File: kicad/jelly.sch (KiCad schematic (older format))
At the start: 30 parts, among them M1 PAGER_MOTOR, M2 PAGER_MOTOR, P1 CONN_01X01, P10 CONN_01X01, P11 CONN_01X01, P12 CONN_01X01, P13 CONN_01X01, P14 CONN_01X01, P15 CONN_01X01, P2 CONN_01X01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

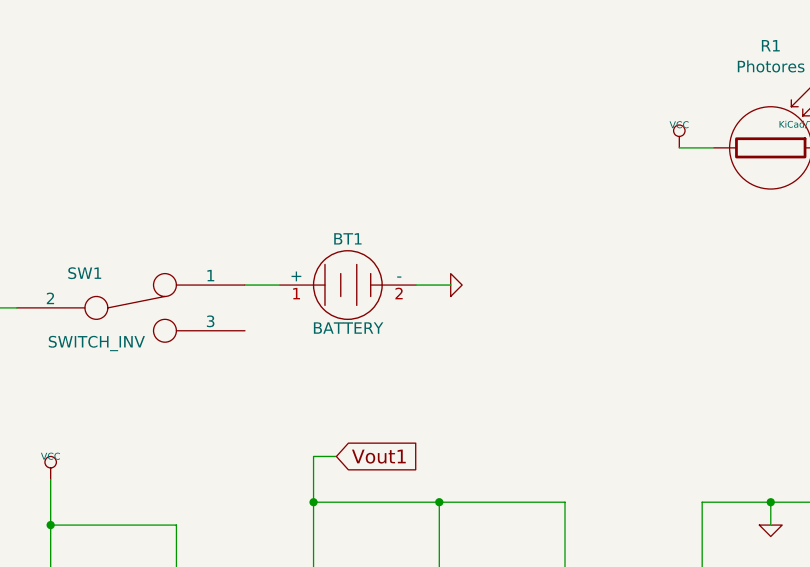
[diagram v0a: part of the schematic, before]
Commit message: Give up on CR2450
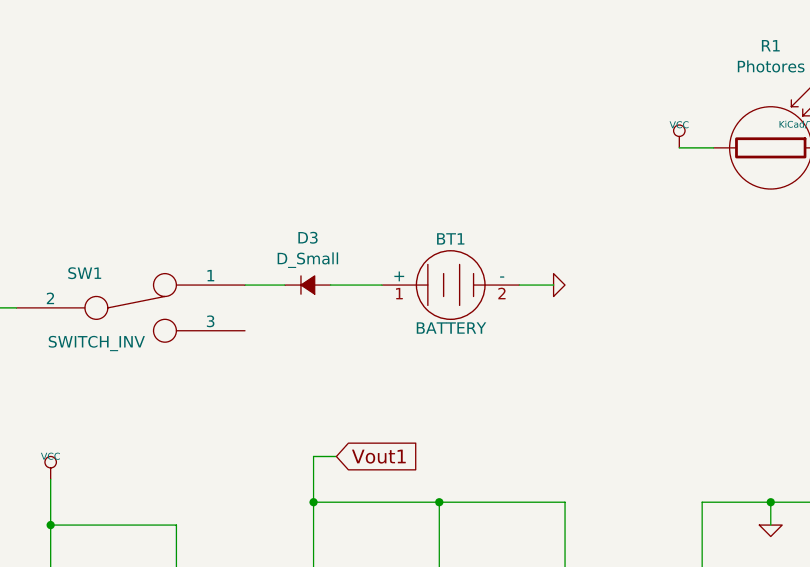
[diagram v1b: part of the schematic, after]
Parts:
- added D3: D_Small, KiCad/Diodes_ThroughHole.pretty:Diode_DO-41_SOD81_Horizontal_RM10, symbol D_Small
- BT1: footprint custom:cr2450_holder -> KiCad/Pin_Headers.pretty:Pin_Header_Straight_1x02
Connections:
- wire segments 48 -> 49
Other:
- moved on the sheet: BT1
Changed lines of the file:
@@
 L BATTERY BT1
 U 1 1 57C0D38C
-P 2750 3500
-F 0 "BT1" H 2750 3700 50  0000 C CNN
-F 1 "BATTERY" H 2750 3310 50  0000 C CNN
-F 2 "custom:cr2450_holder" H 2750 3500 60  0001 C CNN
-F 3 "~" H 2750 3500 60  0000 C CNN
-	1    2750 3500
+P 3200 3500
+F 0 "BT1" H 3200 3700 50  0000 C CNN
+F 1 "BATTERY" H 3200 3310 50  0000 C CNN
+F 2 "KiCad/Pin_Headers.pretty:Pin_Header_Straight_1x02" H 3200 3500 60  0001 C CNN
+F 3 "~" H 3200 3500 60  0000 C CNN
+	1    3200 3500
 	1    0    0    -1
 $EndComp
@@
 L GND-RESCUE-bristle_bot #PWR01
 U 1 1 57C0D38E
-P 3200 3500
-F 0 "#PWR01" H 3200 3500 30  0001 C CNN
-F 1 "GND" H 3200 3430 30  0001 C CNN
-F 2 "" H 3200 3500 60  0000 C CNN
-F 3 "" H 3200 3500 60  0000 C CNN
-	1    3200 3500
+P 3650 3500
+F 0 "#PWR01" H 3650 3500 30  0001 C CNN
+F 1 "GND" H 3650 3430 30  0001 C CNN
+F 2 "" H 3650 3500 60  0000 C CNN
+F 3 "" H 3650 3500 60  0000 C CNN
+	1    3650 3500
 	0    -1   -1   0
 $EndComp
@@
 	5050 2900 5050 3200
 Wire Wire Line
-	3050 3500 3200 3500
+	3500 3500 3650 3500
 Wire Wire Line
 	5350 2500 5350 2700
-Wire Wire Line
-	2450 3500 2300 3500
 Wire Wire Line
 	5050 2900 4850 2900
@@
 Wire Wire Line
 	8300 6350 8450 6350
+$Comp
+L D_Small D3
+U 1 1 57C374D3
+P 2575 3500
+F 0 "D3" H 2575 3705 50  0000 C CNN
+F 1 "D_Small" H 2575 3614 50  0000 C CNN
+F 2 "KiCad/Diodes_ThroughHole.pretty:Diode_DO-41_SOD81_Horizontal_RM10" V 2575 3500 50  0001 C CNN
+F 3 "" V 2575 3500 50  0000 C CNN
+	1    2575 3500
+	1    0    0    -1
+$EndComp
+Wire Wire Line
+	2300 3500 2475 3500
+Wire Wire Line
+	2675 3500 2900 3500
 $EndSCHEMATC

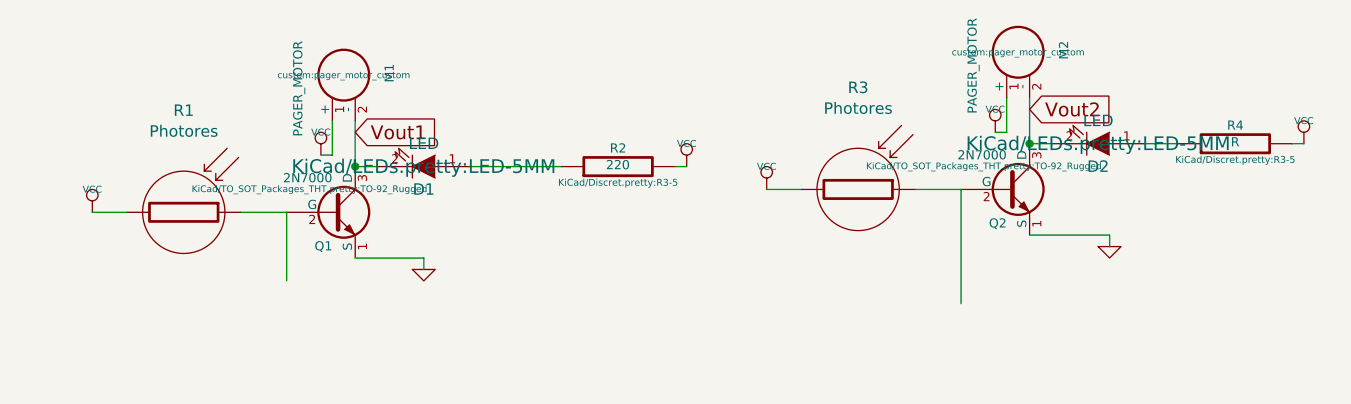
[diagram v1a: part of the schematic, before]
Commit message: Turn of visibility of footprint fields in schematic
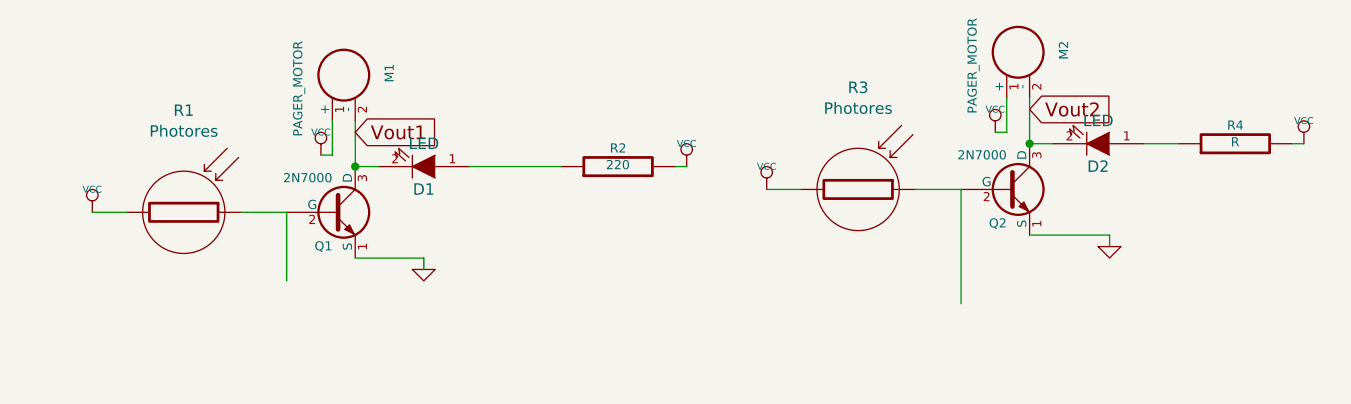
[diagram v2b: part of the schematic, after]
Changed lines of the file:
@@
 F 0 "BT1" H 3200 3700 50  0000 C CNN
 F 1 "BATTERY" H 3200 3310 50  0000 C CNN
-F 2 "KiCad/Pin_Headers.pretty:Pin_Header_Straight_1x02" H 3200 3500 60  0001 C CNN
+F 2 "KiCad/Pin_Headers.pretty:Pin_Header_Straight_1x02" H 3200 3500 29  0001 C CNN
 F 3 "~" H 3200 3500 60  0000 C CNN
 	1    3200 3500
@@
 F 0 "M1" V 5500 2350 40  0000 R CNN
 F 1 "PAGER_MOTOR" V 5100 2450 40  0000 R CNN
-F 2 "custom:pager_motor_custom" H 5300 2300 29  0000 C CNN
+F 2 "custom:pager_motor_custom" H 5300 2300 29  0001 C CNN
 F 3 "" H 5300 2300 60  0000 C CNN
 	1    5300 2300
@@
 F 0 "Q1" H 5250 2752 40  0000 R CNN
 F 1 "2N7000" H 5250 3050 40  0000 R CNN
-F 2 "KiCad/TO_SOT_Packages_THT.pretty:TO-92_Rugged" H 5150 3002 29  0000 C CNN
+F 2 "KiCad/TO_SOT_Packages_THT.pretty:TO-92_Rugged" H 5150 3002 29  0001 C CNN
 F 3 "" H 5250 2900 60  0000 C CNN
 	1    5250 2900
@@
 F 0 "#PWR02" H 1100 3700 30  0001 C CNN
 F 1 "VCC" H 1100 3700 30  0000 C CNN
-F 2 "" H 1100 3600 60  0000 C CNN
+F 2 "" H 1100 3600 60  0001 C CNN
 F 3 "" H 1100 3600 60  0000 C CNN
 	1    1100 3600
@@
 F 0 "#PWR03" H 4200 3000 30  0001 C CNN
 F 1 "VCC" H 4200 3000 30  0000 C CNN
-F 2 "" H 4200 2900 60  0000 C CNN
+F 2 "" H 4200 2900 60  0001 C CNN
 F 3 "" H 4200 2900 60  0000 C CNN
 	1    4200 2900
@@
 F 0 "#PWR04" H 5200 2750 30  0001 C CNN
 F 1 "VCC" H 5200 2750 30  0000 C CNN
-F 2 "" H 5200 2650 60  0000 C CNN
+F 2 "" H 5200 2650 60  0001 C CNN
 F 3 "" H 5200 2650 60  0000 C CNN
 	1    5200 2650
@@
 F 0 "#PWR05" H 5650 3150 30  0001 C CNN
 F 1 "GND" H 5650 3080 30  0001 C CNN
-F 2 "" H 5650 3150 60  0000 C CNN
+F 2 "" H 5650 3150 60  0001 C CNN
 F 3 "" H 5650 3150 60  0000 C CNN
 	1    5650 3150
@@
 F 0 "M2" V 8450 2250 40  0000 R CNN
 F 1 "PAGER_MOTOR" V 8050 2350 40  0000 R CNN
-F 2 "custom:pager_motor_custom" H 8250 2200 29  0000 C CNN
+F 2 "custom:pager_motor_custom" H 8250 2200 29  0001 C CNN
 F 3 "" H 8250 2200 60  0000 C CNN
 	1    8250 2200
@@
 F 0 "#PWR06" H 8150 2650 30  0001 C CNN
 F 1 "VCC" H 8150 2650 30  0000 C CNN
-F 2 "" H 8150 2550 60  0000 C CNN
+F 2 "" H 8150 2550 60  0001 C CNN
 F 3 "" H 8150 2550 60  0000 C CNN
 	1    8150 2550
@@
 F 0 "Q2" H 8200 2652 40  0000 R CNN
 F 1 "2N7000" H 8200 2950 40  0000 R CNN
-F 2 "KiCad/TO_SOT_Packages_THT.pretty:TO-92_Rugged" H 8100 2902 29  0000 C CNN
+F 2 "KiCad/TO_SOT_Packages_THT.pretty:TO-92_Rugged" H 8100 2902 29  0001 C CNN
 F 3 "" H 8200 2800 60  0000 C CNN
 	1    8200 2800
@@
 F 0 "#PWR07" H 8650 3050 30  0001 C CNN
 F 1 "GND" H 8650 2980 30  0001 C CNN
-F 2 "" H 8650 3050 60  0000 C CNN
+F 2 "" H 8650 3050 60  0001 C CNN
 F 3 "" H 8650 3050 60  0000 C CNN
 	1    8650 3050
@@
 F 0 "#PWR08" H 7150 2900 30  0001 C CNN
 F 1 "VCC" H 7150 2900 30  0000 C CNN
-F 2 "" H 7150 2800 60  0000 C CNN
+F 2 "" H 7150 2800 60  0001 C CNN
 F 3 "" H 7150 2800 60  0000 C CNN
 	1    7150 2800
@@
 F 0 "D2" H 8600 2700 50  0000 C CNN
 F 1 "LED" H 8600 2500 50  0000 C CNN
-F 2 "KiCad/LEDs.pretty:LED-5MM" H 8600 2600 60  0000 C CNN
+F 2 "KiCad/LEDs.pretty:LED-5MM" H 8600 2600 29  0001 C CNN
 F 3 "~" H 8600 2600 60  0000 C CNN
 	1    8600 2600
@@
 F 0 "R4" V 9280 2600 40  0000 C CNN
 F 1 "R" V 9207 2601 40  0000 C CNN
-F 2 "KiCad/Discret.pretty:R3-5" V 9130 2600 30  0000 C CNN
+F 2 "KiCad/Discret.pretty:R3-5" V 9130 2600 30  0001 C CNN
 F 3 "~" H 9200 2600 30  0000 C CNN
 	1    9200 2600
@@
 F 0 "#PWR09" H 9500 2700 30  0001 C CNN
 F 1 "VCC" H 9500 2700 30  0000 C CNN
-F 2 "" H 9500 2600 60  0000 C CNN
+F 2 "" H 9500 2600 60  0001 C CNN
 F 3 "" H 9500 2600 60  0000 C CNN
 	1    9500 2600
@@
 F 0 "R2" V 6580 2700 40  0000 C CNN
 F 1 "220" V 6507 2701 40  0000 C CNN
-F 2 "KiCad/Discret.pretty:R3-5" V 6430 2700 30  0000 C CNN
+F 2 "KiCad/Discret.pretty:R3-5" V 6430 2700 30  0001 C CNN
 F 3 "~" H 6500 2700 30  0000 C CNN
 	1    6500 2700
@@
 F 0 "D1" H 5650 2800 50  0000 C CNN
 F 1 "LED" H 5650 2600 50  0000 C CNN
-F 2 "KiCad/LEDs.pretty:LED-5MM" H 5650 2700 60  0000 C CNN
+F 2 "KiCad/LEDs.pretty:LED-5MM" H 5650 2700 60  0001 C CNN
 F 3 "~" H 5650 2700 60  0000 C CNN
 	1    5650 2700
@@
 F 0 "#PWR010" H 6800 2800 30  0001 C CNN
 F 1 "VCC" H 6800 2800 30  0000 C CNN
-F 2 "" H 6800 2700 60  0000 C CNN
+F 2 "" H 6800 2700 60  0001 C CNN
 F 3 "" H 6800 2700 60  0000 C CNN
 	1    6800 2700
@@
 F 0 "#PWR011" H 1450 4450 30  0001 C CNN
 F 1 "VCC" H 1450 4450 30  0000 C CNN
-F 2 "" H 1450 4350 60  0000 C CNN
+F 2 "" H 1450 4350 60  0001 C CNN
 F 3 "" H 1450 4350 60  0000 C CNN
 	1    1450 4350
@@
 F 0 "#PWR012" H 7900 4700 30  0001 C CNN
 F 1 "VCC" H 7900 4700 30  0000 C CNN
-F 2 "" H 7900 4600 60  0000 C CNN
+F 2 "" H 7900 4600 60  0001 C CNN
 F 3 "" H 7900 4600 60  0000 C CNN
 	1    7900 4600
@@
 F 0 "#PWR013" H 4600 4550 30  0001 C CNN
 F 1 "GND" H 4600 4480 30  0001 C CNN
-F 2 "" H 4600 4550 60  0000 C CNN
+F 2 "" H 4600 4550 60  0001 C CNN
 F 3 "" H 4600 4550 60  0000 C CNN
 	1    4600 4550
@@
 F 0 "#PWR014" H 8450 6450 30  0001 C CNN
 F 1 "VCC" H 8450 6450 30  0000 C CNN
-F 2 "" H 8450 6350 60  0000 C CNN
+F 2 "" H 8450 6350 60  0001 C CNN
 F 3 "" H 8450 6350 60  0000 C CNN
 	1    8450 6350

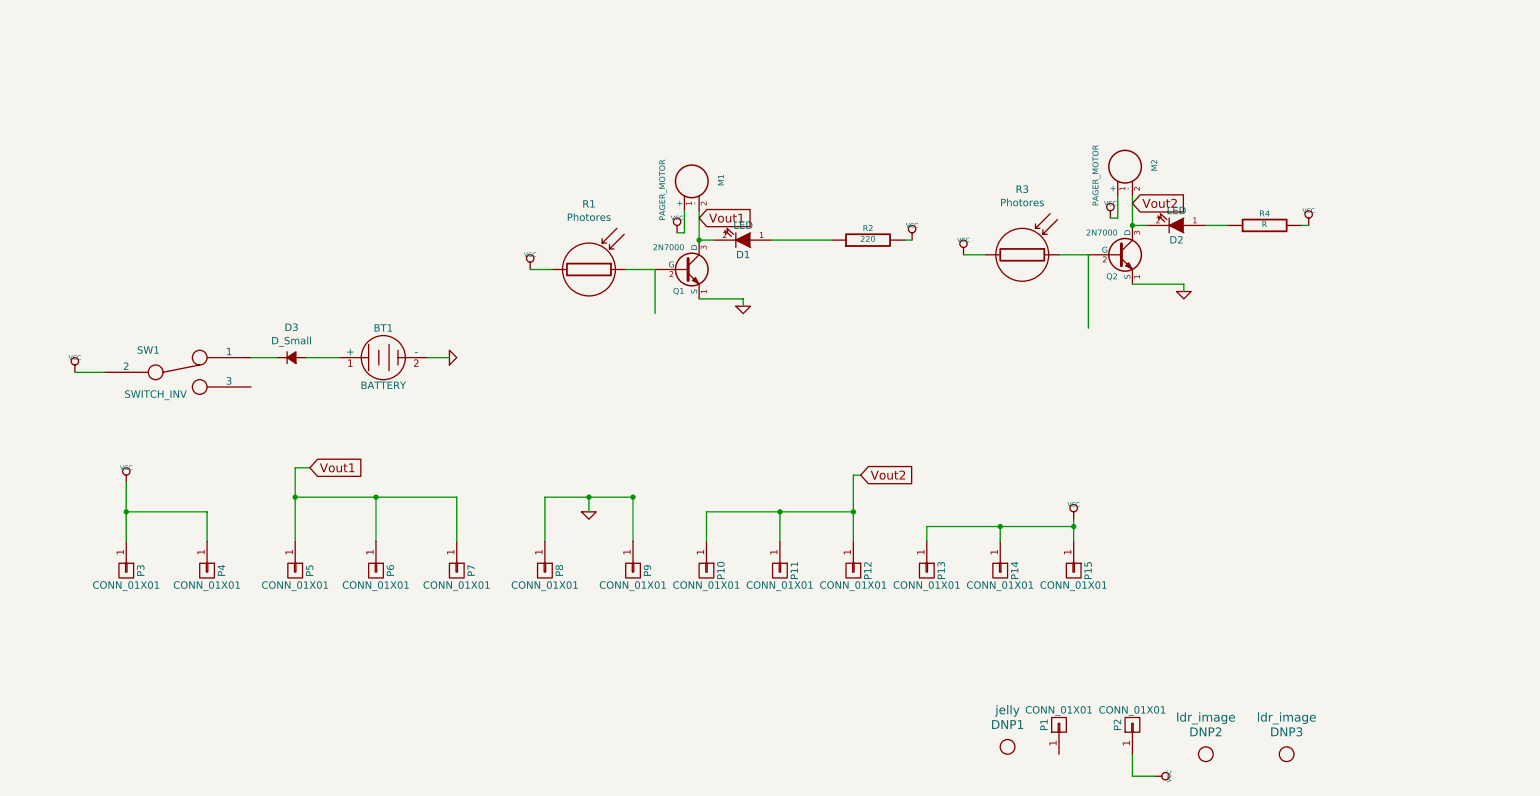
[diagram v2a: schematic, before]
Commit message: Add tilt switch and work out transistor choice
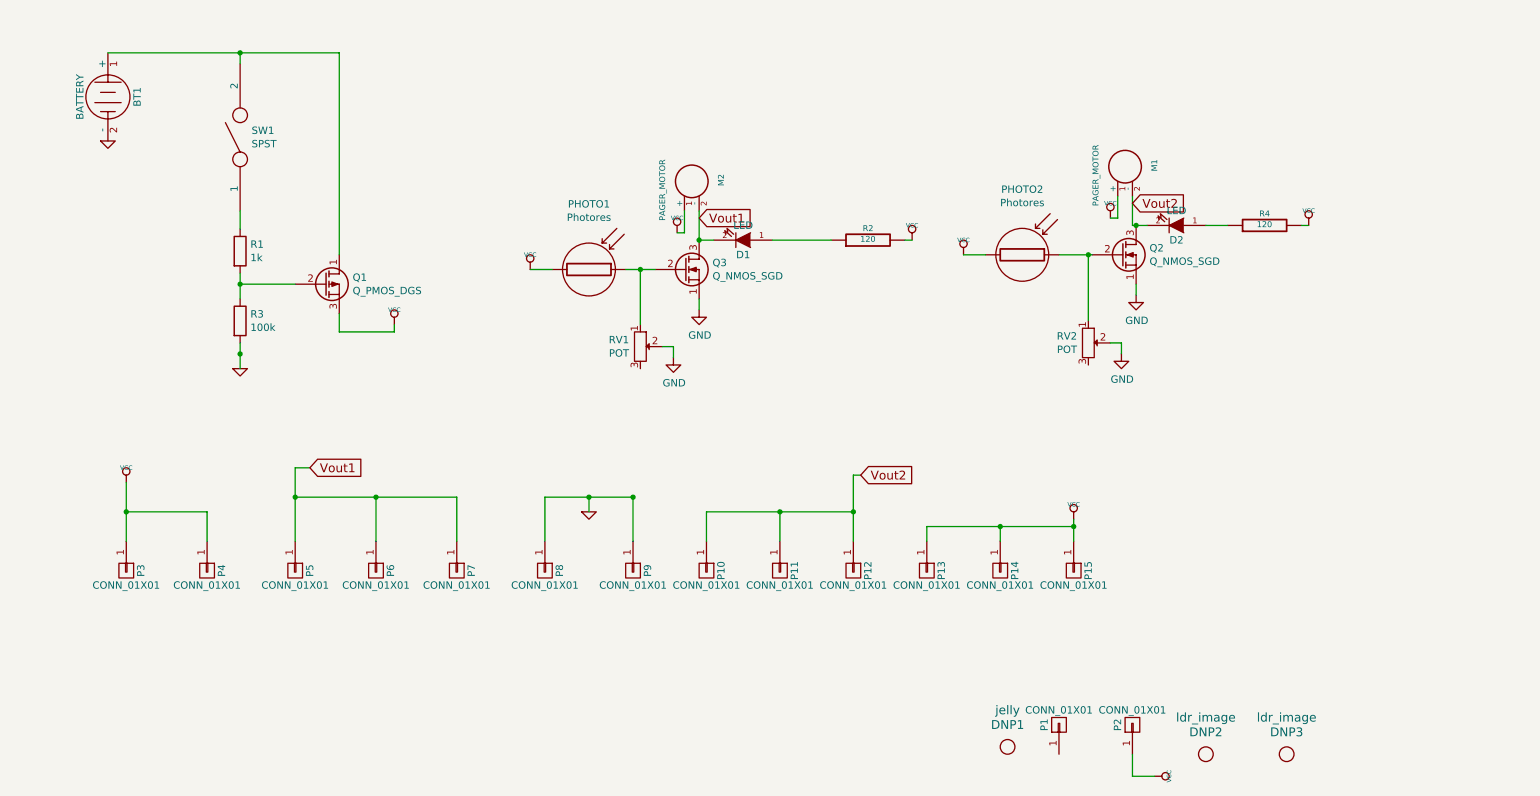
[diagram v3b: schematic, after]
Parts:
- removed D3: D_Small, KiCad/Diodes_ThroughHole.pretty:Diode_DO-41_SOD81_Horizontal_RM10, symbol D_Small
- removed Q1, Q2: 2N7000, KiCad/TO_SOT_Packages_THT.pretty:TO-92_Rugged, symbol 2N7000
- removed SW1: SWITCH_INV, symbol SWITCH_INV
- added Q1: Q_PMOS_DGS, symbol Q_PMOS_DGS
- added Q2, Q3: Q_NMOS_SGD, KiCad/TO_SOT_Packages_THT.pretty:TO-92_Rugged, symbol Q_NMOS_SGD
- added R1: 1k, KiCad/Discret.pretty:R3-5, symbol R
- added R3: 100k, KiCad/Discret.pretty:R3-5, symbol R
- added RV1, RV2: POT, symbol POT
- added SW1: SPST, KiCad/Pin_Headers.pretty:Pin_Header_Straight_1x02, symbol SPST
- D1, D2: Farnell (none) -> 2112111
- R2: value 220 -> 120
- R4: value R -> 120
- renumbered M2 to M1, M1 to M2, R1 to PHOTO1, R3 to PHOTO2
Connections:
- wire segments 49 -> 57
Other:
- moved on the sheet: BT1

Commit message: Switch to low side switch and layout about
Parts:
- removed Q1: Q_PMOS_DGS, symbol Q_PMOS_DGS
- added Q1: Q_NMOS_SGD, KiCad/TO_SOT_Packages_THT.pretty:TO-92_Rugged, symbol Q_NMOS_SGD
- RV1, RV2: footprint (none) -> KiCad/Potentiometers.pretty:Potentiometer_Triwood_RM-065
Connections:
- net GND: now also Q1.1 (S); no longer BT1.2 (-)
- net VCC: now also BT1.1 (+), SW1.2
- net at R1.2, R3.1: now also Q1.2 (G)
- new net: BT1.2 (-), Q1.3 (D)

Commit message: Route
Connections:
- net GND: now also P1.1 (P1)
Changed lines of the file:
@@
 Wire Wire Line
 	1325 2700 1325 2025
+$Comp
+L GND-RESCUE-bristle_bot #PWR?
+U 1 1 57F92FC8
+P 7800 6275
+F 0 "#PWR?" H 7800 6275 30  0001 C CNN
+F 1 "GND" H 7800 6205 30  0001 C CNN
+F 2 "" H 7800 6275 60  0000 C CNN
+F 3 "" H 7800 6275 60  0000 C CNN
+	1    7800 6275
+	1    0    0    -1
+$EndComp
+Wire Wire Line
+	7800 6200 7800 6275
 $EndSCHEMATC
